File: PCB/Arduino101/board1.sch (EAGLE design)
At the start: 1 part

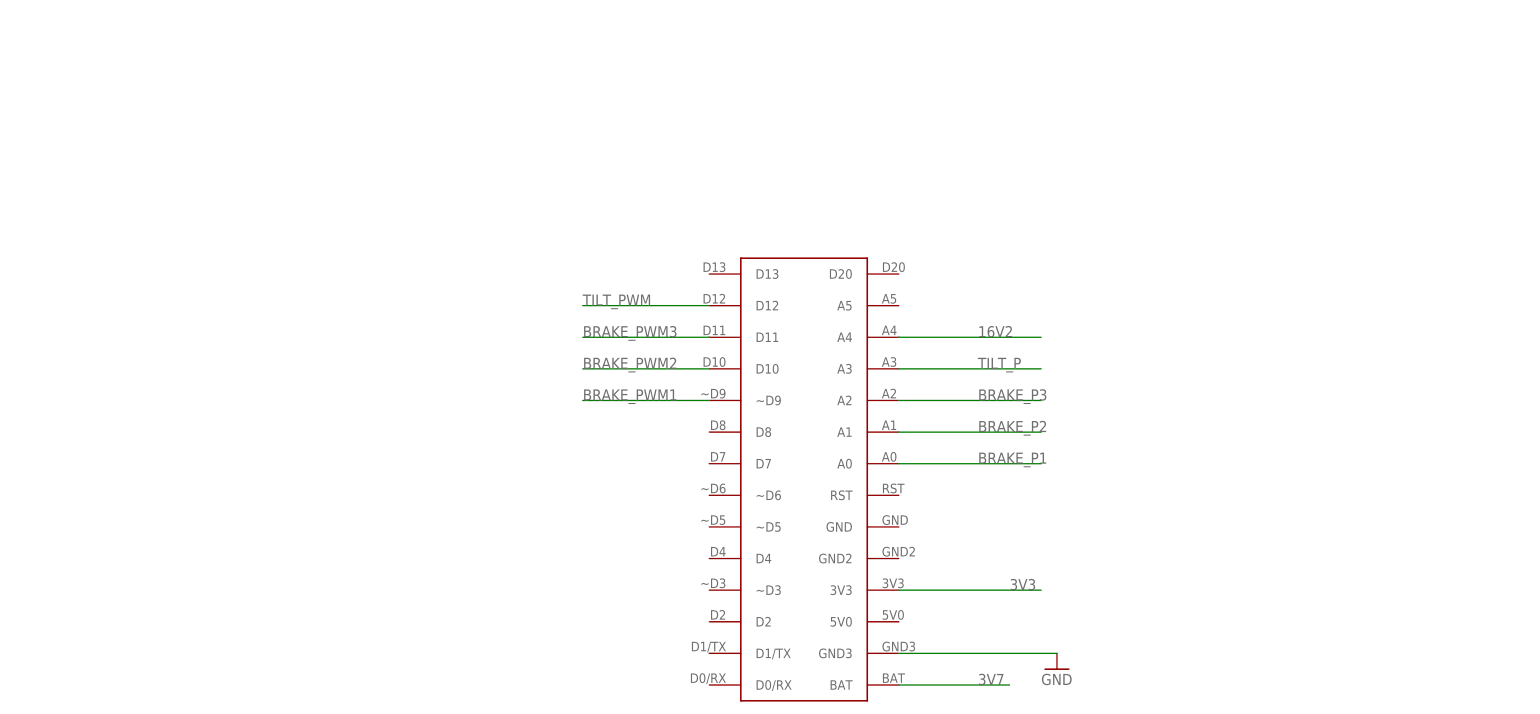
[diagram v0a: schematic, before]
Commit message: schematic v1 and layed out components
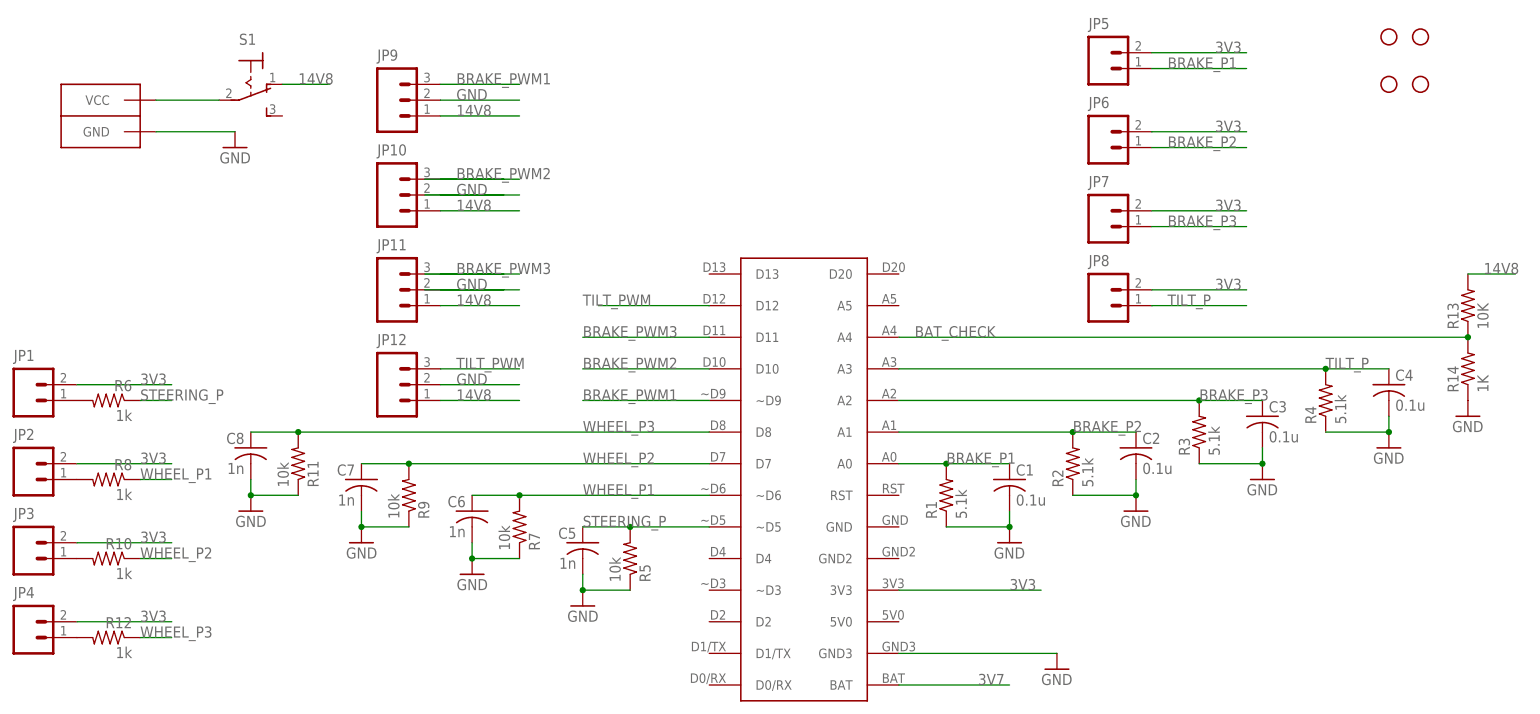
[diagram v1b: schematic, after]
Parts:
- added C1, C2, C3, C4: 0.1u, adafruit:C-USC0805
- added C5, C6, C7, C8: 1n, adafruit:C-USC0805
- added CONN1: ANDERSONHORIZONTAL, ee192:ANDERSONHORIZONTAL
- added JP1, JP2, JP3, JP4, JP5, JP6, JP7, JP8: (no value), ee192:M02PTH
- added JP10, JP11, JP12, JP9: (no value), ee192:M03PTH
- added JP13, JP14, JP15, JP16: STAND-OFF, ee192:STAND-OFF
- added R1, R2, R3, R4: 5.1k, resistor:R-US_R0805
- added R10, R12, R6, R8: 1k, resistor:R-US_R0805
- added R11, R5, R7, R9: 10k, resistor:R-US_R0805
- added R13: 10K, resistor:R-US_R0805
- added R14: 1K, resistor:R-US_R0805
- added S1: (no value), switch:320-916
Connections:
- removed net 16V2: U$1.A4
- new net 14V8: JP10.1, JP11.1, JP12.1, JP9.1, R13.2, S1.O
- new net BAT_CHECK: R13.1, R14.2, U$1.A4
- new net N$1: JP1.1, R6.2
- new net N$2: JP2.1, R8.2
- new net N$3: JP3.1, R10.2
- new net N$4: JP4.1, R12.2
- new net N$5: CONN1.VCC, S1.P
- new net STEERING_P: C5.1, R5.2, R6.1, U$1.~D5
- new net WHEEL_P1: C6.1, R7.2, R8.1, U$1.~D6
- new net WHEEL_P2: C7.1, R10.1, R9.2, U$1.D7
- new net WHEEL_P3: C8.1, R11.2, R12.1, U$1.D8
- net 3V3: now also JP1.2, JP2.2, JP3.2, JP4.2, JP5.2, JP6.2, JP7.2, JP8.2
- net BRAKE_P1: now also C1.1, JP5.1, R1.2
- net BRAKE_P2: now also C2.1, JP6.1, R2.2
- net BRAKE_P3: now also C3.1, JP7.1, R3.2
- net BRAKE_PWM1: now also JP9.3
- net BRAKE_PWM2: now also JP10.3
- net BRAKE_PWM3: now also JP11.3
- net GND: now also C1.2, C2.2, C3.2, C4.2, C5.2, C6.2, C7.2, C8.2, CONN1.GND, JP10.2, JP11.2, JP12.2, JP9.2, R1.1, R11.1, R14.1, R2.1, R3.1, R4.1, R5.1, R7.1, R9.1
- net TILT_P: now also C4.1, JP8.1, R4.2
- net TILT_PWM: now also JP12.3
